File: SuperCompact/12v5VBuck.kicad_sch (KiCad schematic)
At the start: 16 parts, among them IC1 TPS54302DDCT, J1 Conn_01x02, J2 Conn_01x02

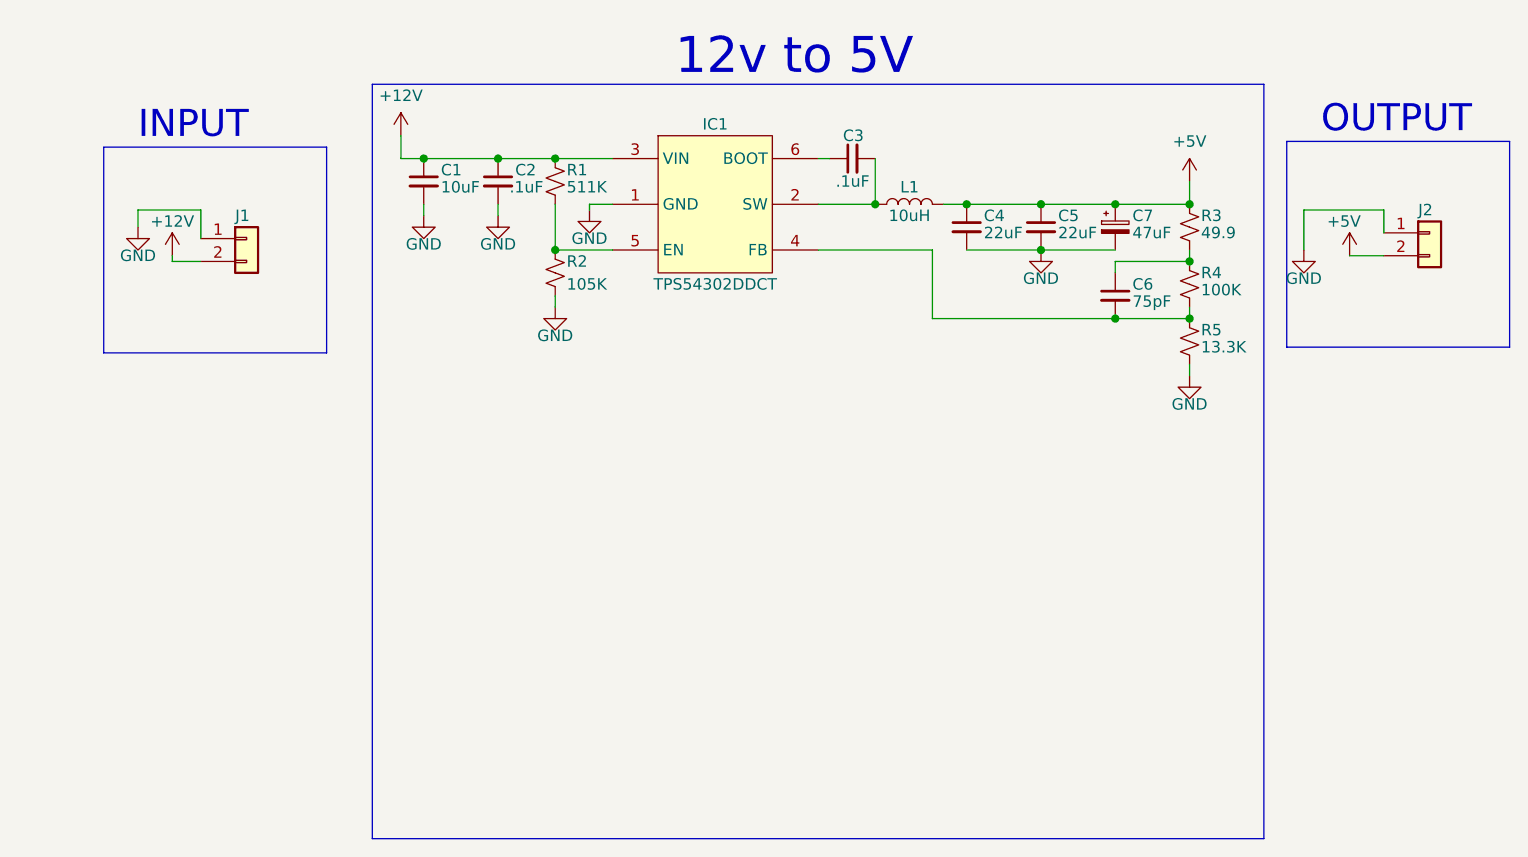
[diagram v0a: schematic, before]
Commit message: Added bypass capacitor to input
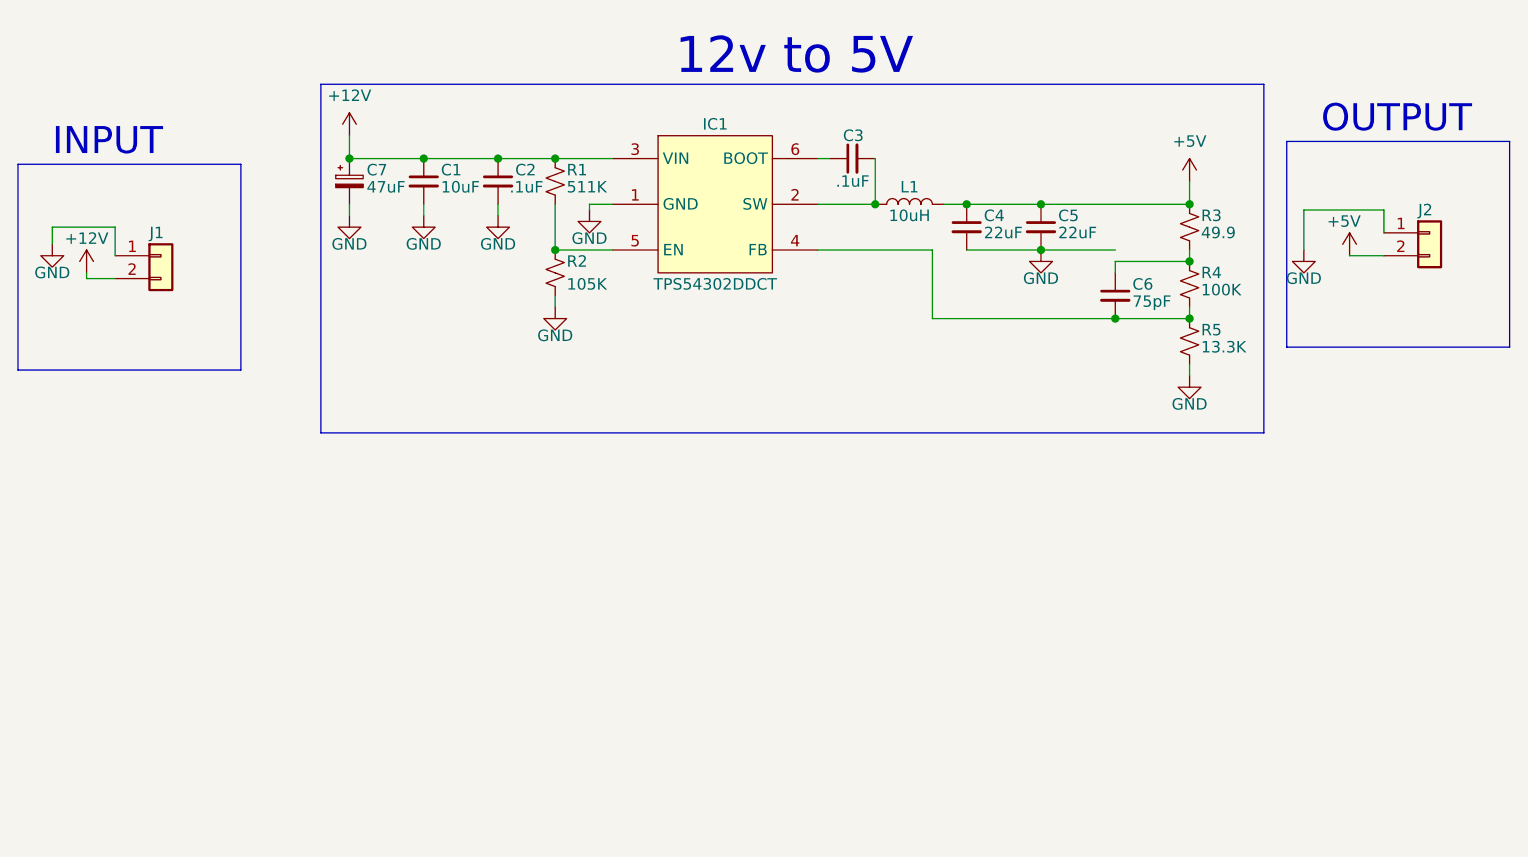
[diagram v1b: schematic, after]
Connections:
- net +12V: now also C7.1
- net +5V: no longer C7.1
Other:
- moved on the sheet: J1
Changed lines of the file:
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@@
   (junction (at 177.165 70.485) (diameter 0) (color 0 0 0 0)
   )
-  (junction (at 185.42 70.485) (diameter 0) (color 0 0 0 0)
-  )
   (junction (at 193.675 70.485) (diameter 0) (color 0 0 0 0)
   )
+  (junction (at 100.33 65.405) (diameter 0) (color 0 0 0 0)
+  )
   (junction (at 123.19 75.565) (diameter 0) (color 0 0 0 0)
   )
@@
     (stroke (width 0) (type default))
   )
-  (wire (pts (xy 83.82 71.12) (xy 83.82 74.295))
+  (wire (pts (xy 74.295 73.025) (xy 74.295 76.2))
     (stroke (width 0) (type default))
   )
@@
     (stroke (width 0) (type default))
   )
+  (wire (pts (xy 100.33 70.485) (xy 100.33 71.755))
+    (stroke (width 0) (type default))
+  )
   (wire (pts (xy 123.19 80.645) (xy 123.19 81.915))
     (stroke (width 0) (type default))
@@
     (stroke (width 0) (type default))
   )
-  (wire (pts (xy 76.835 71.12) (xy 83.82 71.12))
+  (wire (pts (xy 67.31 73.025) (xy 74.295 73.025))
     (stroke (width 0) (type default))
   )
@@
     (stroke (width 0) (type default))
   )
-  (wire (pts (xy 106.045 65.405) (xy 106.045 62.865))
-    (stroke (width 0) (type default))
-  )
-  (wire (pts (xy 177.165 70.485) (xy 185.42 70.485))
+  (wire (pts (xy 100.33 65.405) (xy 108.585 65.405))
+    (stroke (width 0) (type default))
+  )
+  (wire (pts (xy 100.33 65.405) (xy 100.33 62.865))
+    (stroke (width 0) (type default))
+  )
+  (wire (pts (xy 177.165 70.485) (xy 193.675 70.485))
     (stroke (width 0) (type default))
   )
@@
     (stroke (width 0) (type default))
   )
-  (wire (pts (xy 185.42 70.485) (xy 193.675 70.485))
-    (stroke (width 0) (type default))
-  )
-  (wire (pts (xy 80.645 76.2) (xy 80.645 76.835))
+  (wire (pts (xy 71.12 78.105) (xy 71.12 78.74))
     (stroke (width 0) (type default))
   )
@@
     (stroke (width 0) (type default))
   )
-  (wire (pts (xy 83.82 76.835) (xy 80.645 76.835))
+  (wire (pts (xy 74.295 78.74) (xy 71.12 78.74))
     (stroke (width 0) (type default))
   )
@@
     (stroke (width 0) (type default))
   )
-  (wire (pts (xy 76.835 71.12) (xy 76.835 73.025))
+  (wire (pts (xy 67.31 73.025) (xy 67.31 74.93))
     (stroke (width 0) (type default))
   )
@@
     (stroke (width 0) (type default))
   )
-  (wire (pts (xy 108.585 65.405) (xy 106.045 65.405))
-    (stroke (width 0) (type default))
-  )
   (wire (pts (xy 185.42 83.185) (xy 193.675 83.185))
     (stroke (width 0) (type default))
   )
-  (rectangle (start 73.025 64.135) (end 97.79 86.995)
+  (rectangle (start 63.5 66.04) (end 88.265 88.9)
     (stroke (width 0) (type default))
     (fill (type none))
@@
     (fill (type none))
   )
-  (rectangle (start 102.87 57.15) (end 201.93 140.97)
+  (rectangle (start 97.155 57.15) (end 201.93 95.885)
     (stroke (width 0) (type default))
     (fill (type none))
@@
     (effects (font (size 4 4)) (justify left bottom))
   )
-  (text "INPUT" (at 76.835 63.5 0)
+  (text "INPUT" (at 67.31 65.405 0)
     (effects (font (size 3 3)) (justify left bottom))
   )
@@
     )
   )
+  (symbol (lib_id "power:GND") (at 100.33 71.755 0) (unit 1)
+    (in_bom yes) (on_board yes) (dnp no)
+    (property "Reference" "#PWR013" (at 100.33 78.105 0)
+      (effects (font (size 1.27 1.27)) hide)
+    )
+    (property "Value" "GND" (at 100.33 74.93 0)
+      (effects (font (size 1.27 1.27)))
+    )
+    (property "Footprint" "" (at 100.33 71.755 0)
+      (effects (font (size 1.27 1.27)) hide)
+    )
+    (property "Datasheet" "" (at 100.33 71.755 0)
+      (effects (font (size 1.27 1.27)) hide)
+    )
+    (pin "1")
+    (instances
+      (project "12v5VBuck"
+        (path "/5b52d536-76f3-4180-b70d-b6911106f62c"
+          (reference "#PWR013") (unit 1)
+        )
+      )
+    )
+  )
   (symbol (lib_id "power:GND") (at 108.585 71.755 0) (unit 1)
     (in_bom yes) (on_board yes) (dnp no)
@@
     )
   )
-  (symbol (lib_id "power:+12V") (at 106.045 62.865 0) (unit 1)
+  (symbol (lib_id "power:+12V") (at 100.33 62.865 0) (unit 1)
     (in_bom yes) (on_board yes) (dnp no) (fields_autoplaced)
-    (property "Reference" "#PWR01" (at 106.045 66.675 0)
-      (effects (font (size 1.27 1.27)) hide)
-    )
-    (property "Value" "+12V" (at 106.045 58.42 0)
-      (effects (font (size 1.27 1.27)))
-    )
-    (property "Footprint" "" (at 106.045 62.865 0)
-      (effects (font (size 1.27 1.27)) hide)
-    )
-    (property "Datasheet" "" (at 106.045 62.865 0)
+    (property "Reference" "#PWR01" (at 100.33 66.675 0)
+      (effects (font (size 1.27 1.27)) hide)
+    )
+    (property "Value" "+12V" (at 100.33 58.42 0)
+      (effects (font (size 1.27 1.27)))
+    )
+    (property "Footprint" "" (at 100.33 62.865 0)
+      (effects (font (size 1.27 1.27)) hide)
+    )
+    (property "Datasheet" "" (at 100.33 62.865 0)
       (effects (font (size 1.27 1.27)) hide)
     )
@@
     )
   )
-  (symbol (lib_id "Connector_Generic:Conn_01x02") (at 88.9 74.295 0) (unit 1)
-    (in_bom yes) (on_board yes) (dnp no)
-    (property "Reference" "J1" (at 87.63 71.755 0)
-      (effects (font (size 1.27 1.27)) (justify left))
-    )
-    (property "Value" "Conn_01x02" (at 92.075 76.835 0)
+  (symbol (lib_id "Connector_Generic:Conn_01x02") (at 79.375 76.2 0) (unit 1)
+    (in_bom yes) (on_board yes) (dnp no)
+    (property "Reference" "J1" (at 78.105 73.66 0)
+      (effects (font (size 1.27 1.27)) (justify left))
+    )
+    (property "Value" "Conn_01x02" (at 82.55 78.74 0)
       (effects (font (size 1.27 1.27)) (justify left) hide)
     )
-    (property "Footprint" "footprints:CONN_1984617_PXC" (at 88.9 74.295 0)
-      (effects (font (size 1.27 1.27)) hide)
-    )
-    (property "Datasheet" "https://www.digikey.com/en/products/detail/phoenix-contact/1984617/950849" (at 88.9 74.295 0)
+    (property "Footprint" "footprints:CONN_1984617_PXC" (at 79.375 76.2 0)
+      (effects (font (size 1.27 1.27)) hide)
+    )
+    (property "Datasheet" "https://www.digikey.com/en/products/detail/phoenix-contact/1984617/950849" (at 79.375 76.2 0)
       (effects (font (size 1.27 1.27)) hide)
     )
@@
     )
   )
-  (symbol (lib_id "power:GND") (at 76.835 73.025 0) (unit 1)
-    (in_bom yes) (on_board yes) (dnp no)
-    (property "Reference" "#PWR010" (at 76.835 79.375 0)
-      (effects (font (size 1.27 1.27)) hide)
-    )
-    (property "Value" "GND" (at 76.835 76.2 0)
-      (effects (font (size 1.27 1.27)))
-    )
-    (property "Footprint" "" (at 76.835 73.025 0)
-      (effects (font (size 1.27 1.27)) hide)
-    )
-    (property "Datasheet" "" (at 76.835 73.025 0)
+  (symbol (lib_id "power:GND") (at 67.31 74.93 0) (unit 1)
+    (in_bom yes) (on_board yes) (dnp no)
+    (property "Reference" "#PWR010" (at 67.31 81.28 0)
+      (effects (font (size 1.27 1.27)) hide)
+    )
+    (property "Value" "GND" (at 67.31 78.105 0)
+      (effects (font (size 1.27 1.27)))
+    )
+    (property "Footprint" "" (at 67.31 74.93 0)
+      (effects (font (size 1.27 1.27)) hide)
+    )
+    (property "Datasheet" "" (at 67.31 74.93 0)
       (effects (font (size 1.27 1.27)) hide)
     )
@@
     )
   )
-  (symbol (lib_id "power:+12V") (at 80.645 76.2 0) (unit 1)
-    (in_bom yes) (on_board yes) (dnp no)
-    (property "Reference" "#PWR09" (at 80.645 80.01 0)
-      (effects (font (size 1.27 1.27)) hide)
-    )
-    (property "Value" "+12V" (at 80.645 72.39 0)
-      (effects (font (size 1.27 1.27)))
-    )
-    (property "Footprint" "" (at 80.645 76.2 0)
-      (effects (font (size 1.27 1.27)) hide)
-    )
-    (property "Datasheet" "" (at 80.645 76.2 0)
+  (symbol (lib_id "power:+12V") (at 71.12 78.105 0) (unit 1)
+    (in_bom yes) (on_board yes) (dnp no)
+    (property "Reference" "#PWR09" (at 71.12 81.915 0)
+      (effects (font (size 1.27 1.27)) hide)
+    )
+    (property "Value" "+12V" (at 71.12 74.295 0)
+      (effects (font (size 1.27 1.27)))
+    )
+    (property "Footprint" "" (at 71.12 78.105 0)
+      (effects (font (size 1.27 1.27)) hide)
+    )
+    (property "Datasheet" "" (at 71.12 78.105 0)
       (effects (font (size 1.27 1.27)) hide)
     )
@@
         (path "/5b52d536-76f3-4180-b70d-b6911106f62c"
           (reference "#PWR09") (unit 1)
+        )
+      )
+    )
+  )
+  (symbol (lib_id "Device:C_Polarized_Small") (at 100.33 67.945 0) (unit 1)
+    (in_bom yes) (on_board yes) (dnp no)
+    (property "Reference" "C7" (at 102.235 66.6813 0)
+      (effects (font (size 1.27 1.27)) (justify left))
+    )
+    (property "Value" "47uF" (at 102.235 68.5863 0)
+      (effects (font (size 1.27 1.27)) (justify left))
+    )
+    (property "Footprint" "footprints:CAPPM3216X180N" (at 100.33 67.945 0)
+      (effects (font (size 1.27 1.27)) hide)
+    )
+    (property "Datasheet" "https://www.digikey.com/en/products/detail/kyocera-avx/F931A476KAA/4005057" (at 100.33 67.945 0)
+      (effects (font (size 1.27 1.27)) hide)
+    )
+    (pin "1")
+    (pin "2")
+    (instances
+      (project "12v5VBuck"
+        (path "/5b52d536-76f3-4180-b70d-b6911106f62c"
+          (reference "C7") (unit 1)
         )
       )
@@
         )
       )
-    )
-  )
-  (symbol (lib_id "Device:C_Polarized_Small") (at 185.42 73.025 0) (unit 1)
-    (in_bom yes) (on_board yes) (dnp no)
-    (property "Reference" "C7" (at 187.325 71.7613 0)
-      (effects (font (size 1.27 1.27)) (justify left))
-    )
-    (property "Value" "47uF" (at 187.325 73.6663 0)
-      (effects (font (size 1.27 1.27)) (justify left))
-    )
-    (property "Footprint" "footprints:CAPPM3216X180N" (at 185.42 73.025 0)
-      (effects (font (size 1.27 1.27)) hide)
-    )
-    (property "Datasheet" "https://www.digikey.com/en/products/detail/kyocera-avx/F931A476KAA/4005057" (at 185.42 73.025 0)
-      (effects (font (size 1.27 1.27)) hide)
-    )
-    (pin "1")
-    (pin "2")
-    (instances
-      (project "12v5VBuck"
-        (path "/5b52d536-76f3-4180-b70d-b6911106f62c"
-          (reference "C7") (unit 1)
-        )
-      )
